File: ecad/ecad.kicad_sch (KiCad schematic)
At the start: 59 parts, among them J1 JTAG, J2 USB_C, SW1 Cherry MX, SW10 RotaryEncoder_Switch, SW11 RotaryEncoder_Switch, SW12 Cherry MX, SW13 Cherry MX, SW14 Cherry MX, SW15 RESET, SW2 Cherry MX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

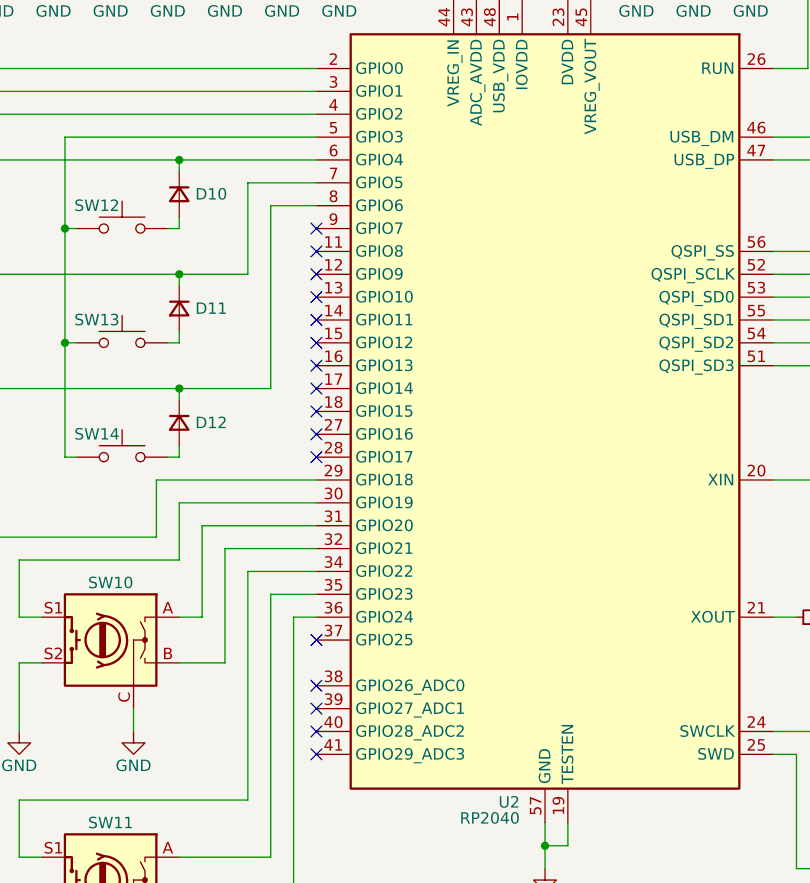
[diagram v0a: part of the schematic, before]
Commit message: feat(ecad): change pcb size to have constant margin
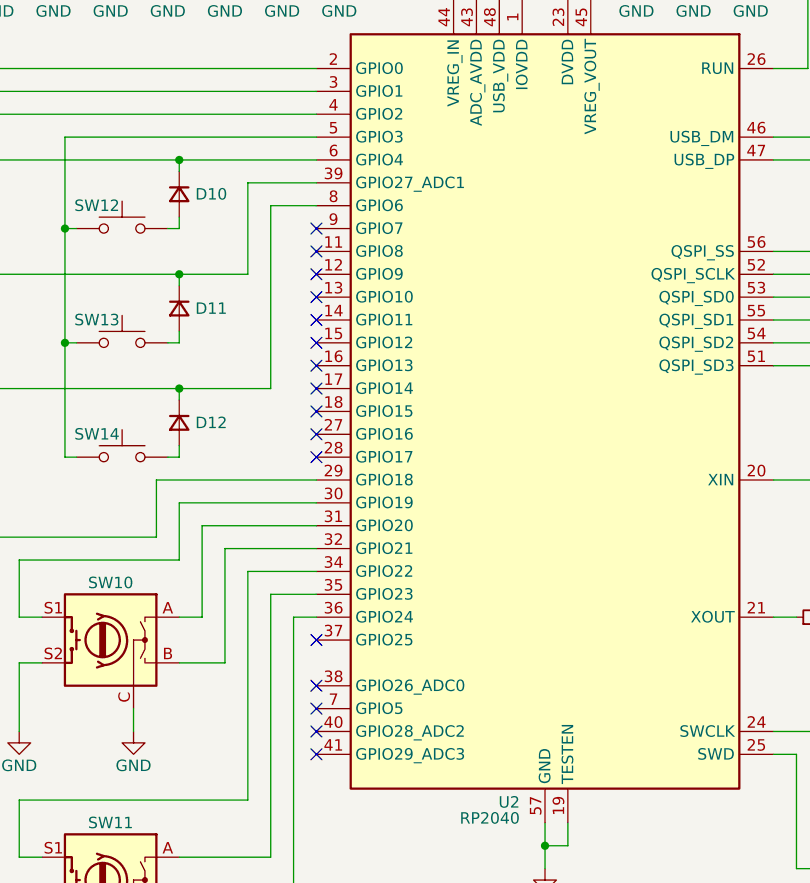
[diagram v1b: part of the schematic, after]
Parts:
- SW1, SW12, SW13, SW14, SW2, SW3, SW4, SW5, SW6, SW7, SW8, SW9: footprint PCM_Switch_Keyboard_Cherry_MX:SW_Cherry_MX_PCB_1.00u -> PCM_Switch_Keyboard_Hotswap_Kailh:SW_Hotswap_Kailh_Choc_V2
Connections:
- net at D11.1 (K), D2.1 (K), D5.1 (K)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: now also U2.39 (GPIO27_ADC1); no longer U2.7 (GPIO5)
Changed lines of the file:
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@@
 			)
 		)
-		(property "Footprint" "PCM_Switch_Keyboard_Cherry_MX:SW_Cherry_MX_PCB_1.00u"
+		(property "Footprint" "PCM_Switch_Keyboard_Hotswap_Kailh:SW_Hotswap_Kailh_Choc_V2"
 			(at 66.04 73.66 0)
 			(effects
@@
 			)
 		)
-		(property "Footprint" "PCM_Switch_Keyboard_Cherry_MX:SW_Cherry_MX_PCB_1.00u"
+		(property "Footprint" "PCM_Switch_Keyboard_Hotswap_Kailh:SW_Hotswap_Kailh_Choc_V2"
 			(at 66.04 60.96 0)
 			(effects
@@
 			)
 		)
-		(property "Footprint" "PCM_Switch_Keyboard_Cherry_MX:SW_Cherry_MX_PCB_1.00u"
+		(property "Footprint" "PCM_Switch_Keyboard_Hotswap_Kailh:SW_Hotswap_Kailh_Choc_V2"
 			(at 40.64 73.66 0)
 			(effects
@@
 			)
 		)
-		(property "Footprint" "PCM_Switch_Keyboard_Cherry_MX:SW_Cherry_MX_PCB_1.00u"
+		(property "Footprint" "PCM_Switch_Keyboard_Hotswap_Kailh:SW_Hotswap_Kailh_Choc_V2"
 			(at 91.44 86.36 0)
 			(effects
@@
 			)
 		)
-		(property "Footprint" "PCM_Switch_Keyboard_Cherry_MX:SW_Cherry_MX_PCB_1.00u"
+		(property "Footprint" "PCM_Switch_Keyboard_Hotswap_Kailh:SW_Hotswap_Kailh_Choc_V2"
 			(at 116.84 86.36 0)
 			(effects
@@
 			)
 		)
-		(property "Footprint" "PCM_Switch_Keyboard_Cherry_MX:SW_Cherry_MX_PCB_1.00u"
+		(property "Footprint" "PCM_Switch_Keyboard_Hotswap_Kailh:SW_Hotswap_Kailh_Choc_V2"
 			(at 116.84 60.96 0)
 			(effects
@@
 			)
 		)
-		(property "Footprint" "PCM_Switch_Keyboard_Cherry_MX:SW_Cherry_MX_PCB_1.00u"
+		(property "Footprint" "PCM_Switch_Keyboard_Hotswap_Kailh:SW_Hotswap_Kailh_Choc_V2"
 			(at 66.04 86.36 0)
 			(effects
@@
 			)
 		)
-		(property "Footprint" "PCM_Switch_Keyboard_Cherry_MX:SW_Cherry_MX_PCB_1.00u"
+		(property "Footprint" "PCM_Switch_Keyboard_Hotswap_Kailh:SW_Hotswap_Kailh_Choc_V2"
 			(at 116.84 73.66 0)
 			(effects
@@
 			)
 		)
-		(property "Footprint" "PCM_Switch_Keyboard_Cherry_MX:SW_Cherry_MX_PCB_1.00u"
+		(property "Footprint" "PCM_Switch_Keyboard_Hotswap_Kailh:SW_Hotswap_Kailh_Choc_V2"
 			(at 40.64 86.36 0)
 			(effects
@@
 			)
 		)
-		(property "Footprint" "PCM_Switch_Keyboard_Cherry_MX:SW_Cherry_MX_PCB_1.00u"
+		(property "Footprint" "PCM_Switch_Keyboard_Hotswap_Kailh:SW_Hotswap_Kailh_Choc_V2"
 			(at 91.44 60.96 0)
 			(effects
@@
 			)
 		)
-		(property "Footprint" "PCM_Switch_Keyboard_Cherry_MX:SW_Cherry_MX_PCB_1.00u"
+		(property "Footprint" "PCM_Switch_Keyboard_Hotswap_Kailh:SW_Hotswap_Kailh_Choc_V2"
 			(at 40.64 60.96 0)
 			(effects
@@
 			)
 		)
-		(property "Footprint" "PCM_Switch_Keyboard_Cherry_MX:SW_Cherry_MX_PCB_1.00u"
+		(property "Footprint" "PCM_Switch_Keyboard_Hotswap_Kailh:SW_Hotswap_Kailh_Choc_V2"
 			(at 91.44 73.66 0)
 			(effects

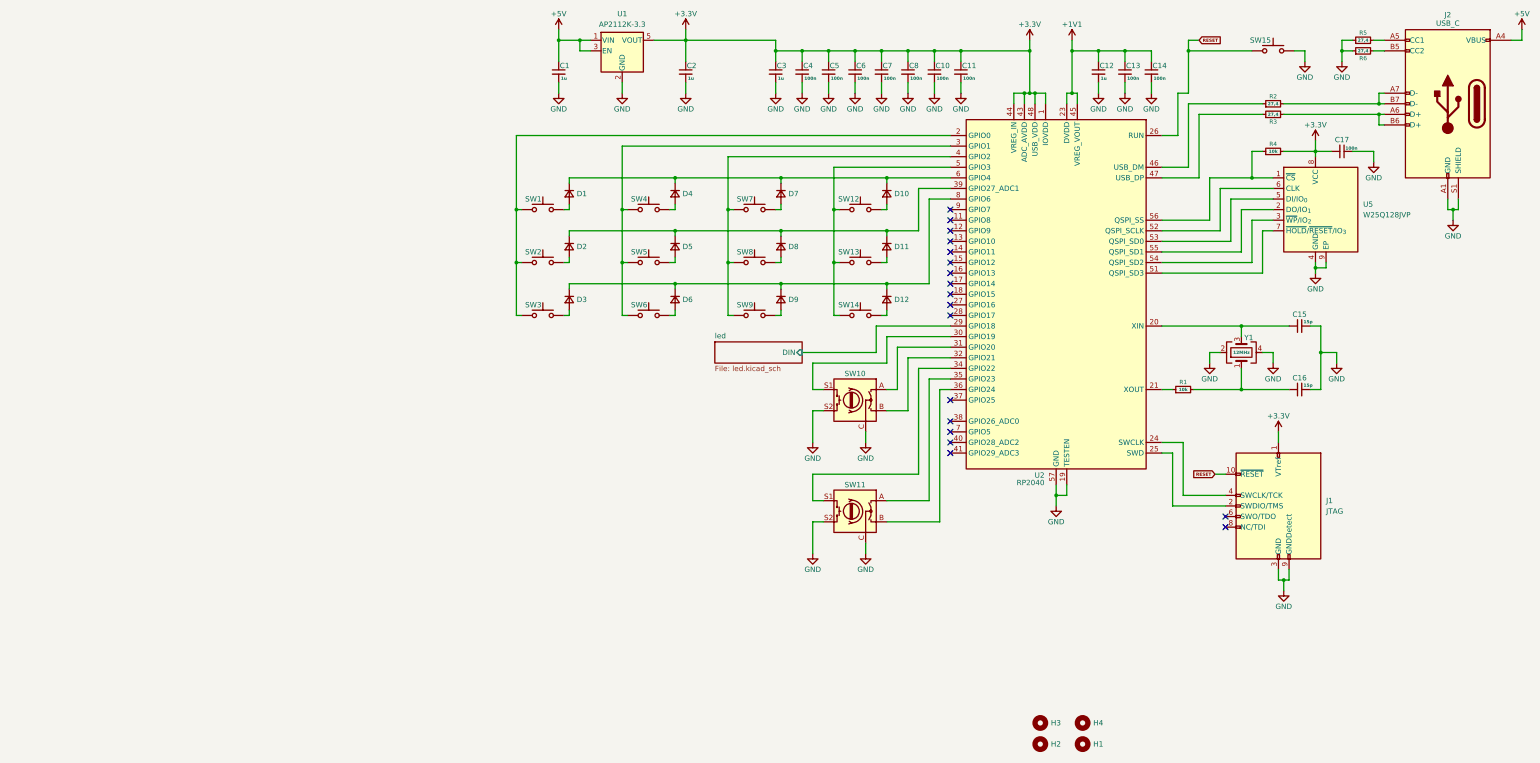
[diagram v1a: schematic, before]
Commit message: fix(ecad): change pcb format
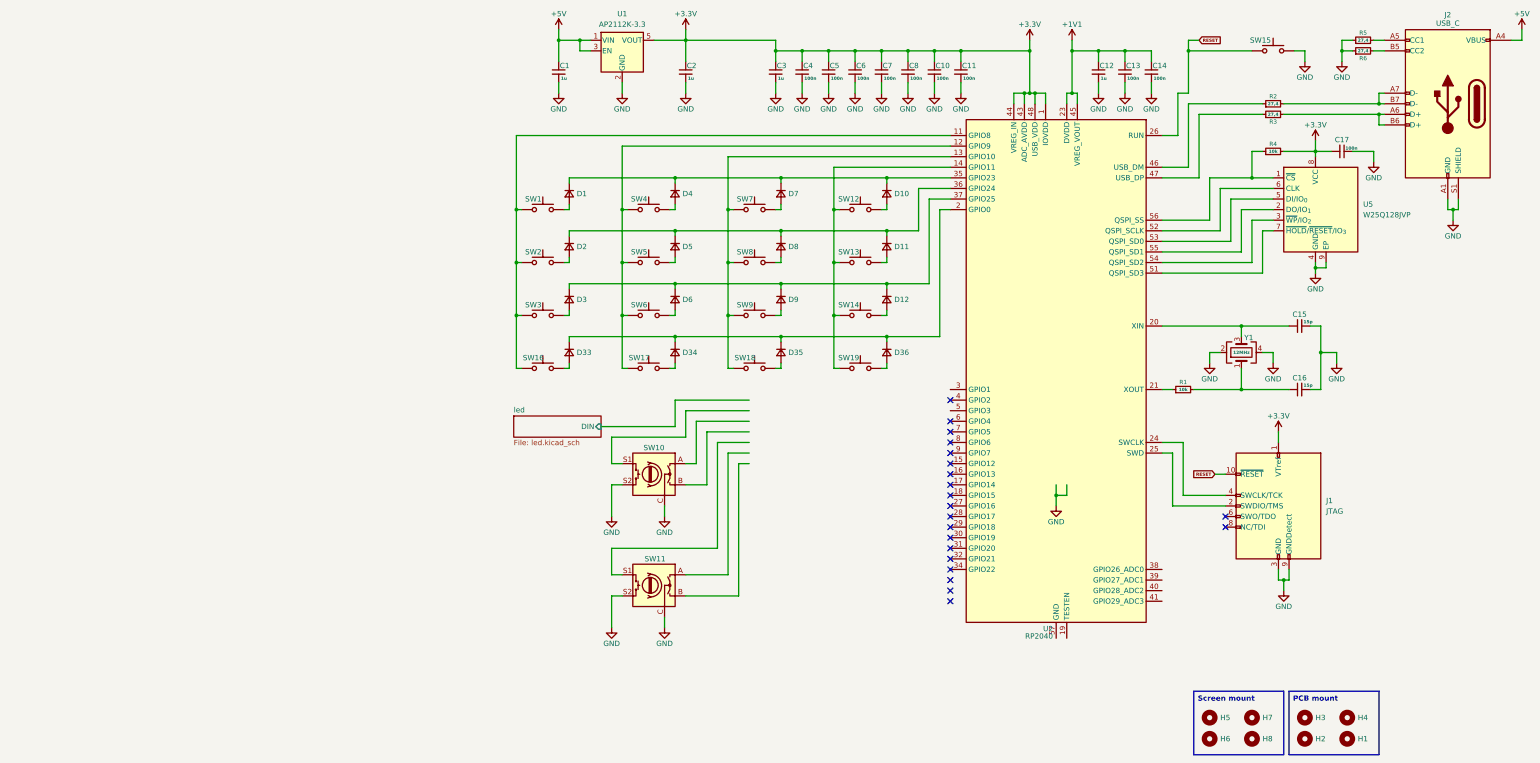
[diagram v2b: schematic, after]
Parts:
- added D33, D34, D35, D36: D_Small, Diode_SMD:D_0402_1005Metric, symbol Device:D_Small
- added H5, H6, H7, H8: MountingHole, MountingHole:MountingHole_2.2mm_M2_DIN965_Pad, symbol Mechanical:MountingHole
- added SW16, SW17, SW18, SW19: Kailh choc v2, PCM_Switch_Keyboard_Hotswap_Kailh:SW_Hotswap_Kailh_Choc_V2, symbol Switch:SW_Push
- H1, H2, H3, H4: footprint MountingHole:MountingHole_2.2mm_M2_DIN965_Pad -> MountingHole:MountingHole_2.2mm_M2_DIN965
- SW1, SW12, SW13, SW14, SW2, SW3, SW4, SW5, SW6, SW7, SW8, SW9: value Cherry MX -> Kailh choc v2
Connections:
- net GND: no longer U2.19 (TESTEN), U2.57 (GND)
- net led/DIN: no longer U2.29 (GPIO18)
- net at SW4.1, SW5.1, SW6.1: now also U2.12 (GPIO9), SW17.1; no longer U2.3 (GPIO1)
- net at D12.1 (K), D3.1 (K), D6.1 (K)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: now also U2.37 (GPIO25); no longer U2.8 (GPIO6)
- net at D11.1 (K), D2.1 (K), D5.1 (K)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: now also U2.36 (GPIO24); no longer U2.39 (GPIO27_ADC1)
- net at SW1.1, SW2.1, SW3.1: now also U2.11 (GPIO8), SW16.1; no longer U2.2 (GPIO0)
- net at SW7.1, SW8.1, SW9.1: now also U2.13 (GPIO10), SW18.1; no longer U2.4 (GPIO2)
- net at D1.1 (K), D10.1 (K), D4.1 (K)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: now also U2.35 (GPIO23); no longer U2.6 (GPIO4)
- net at SW12.1, SW13.1, SW14.1: now also U2.14 (GPIO11), SW19.1; no longer U2.5 (GPIO3)
- net at U2.30 (GPIO19): no longer SW10.S1
- net at U2.31 (GPIO20): no longer SW10.A
- net at U2.32 (GPIO21): no longer SW10.B
- net at U2.34 (GPIO22): no longer SW11.S1
- net at SW11.A: no longer U2.35 (GPIO23)
- net at SW11.B: no longer U2.36 (GPIO24)
- new net: D33.1 (K), D34.1 (K), D35.1 (K), D36.1 (K), U2.2 (GPIO0)
- new net: D35.2 (A), SW18.2
- new net: D33.2 (A), SW16.2
- new net: D34.2 (A), SW17.2
- new net: D36.2 (A), SW19.2
- no-connect marks 18 -> 21
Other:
- moved on the sheet: H1, H2, H4, SW10, SW11, U2

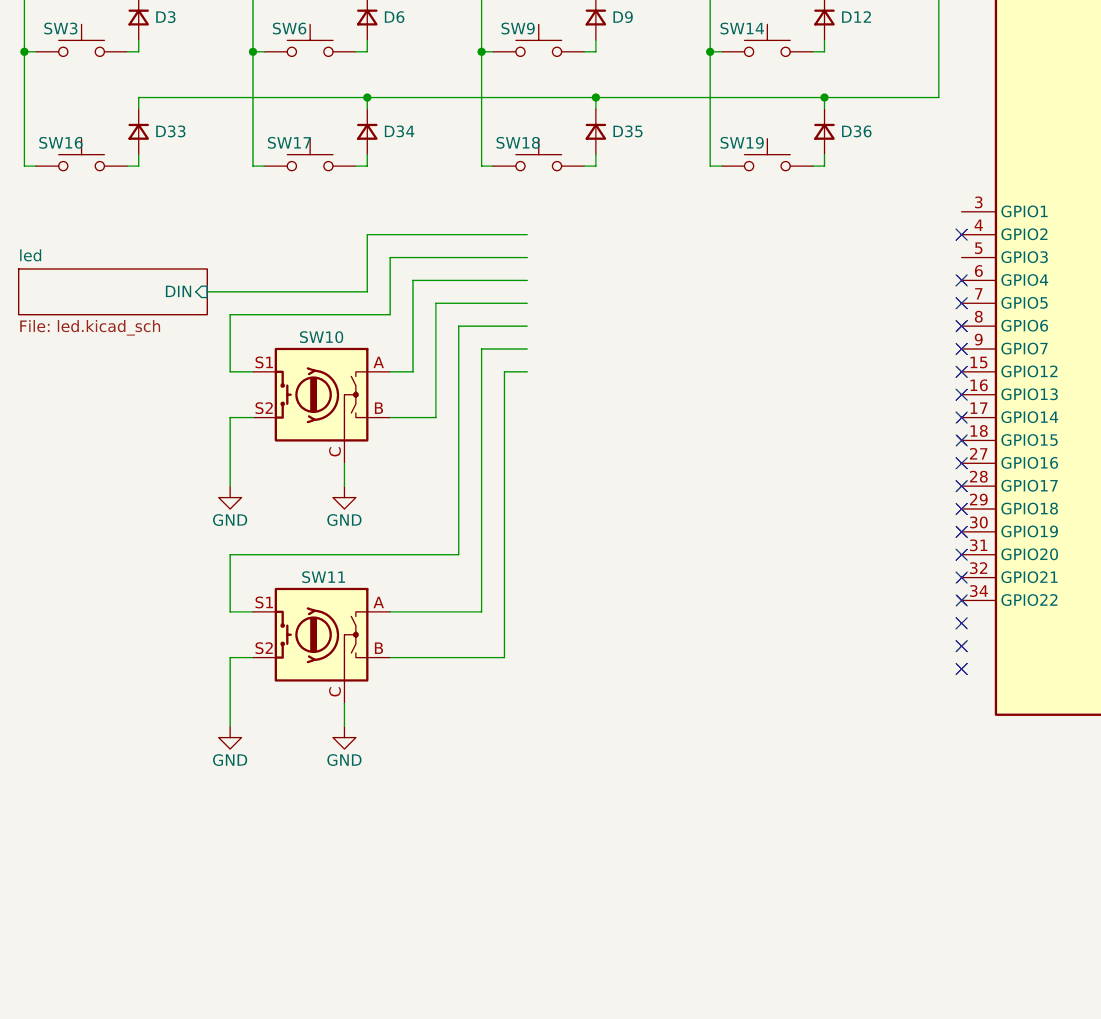
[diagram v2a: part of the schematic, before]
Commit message: fix(ecad): replace components to fit new format
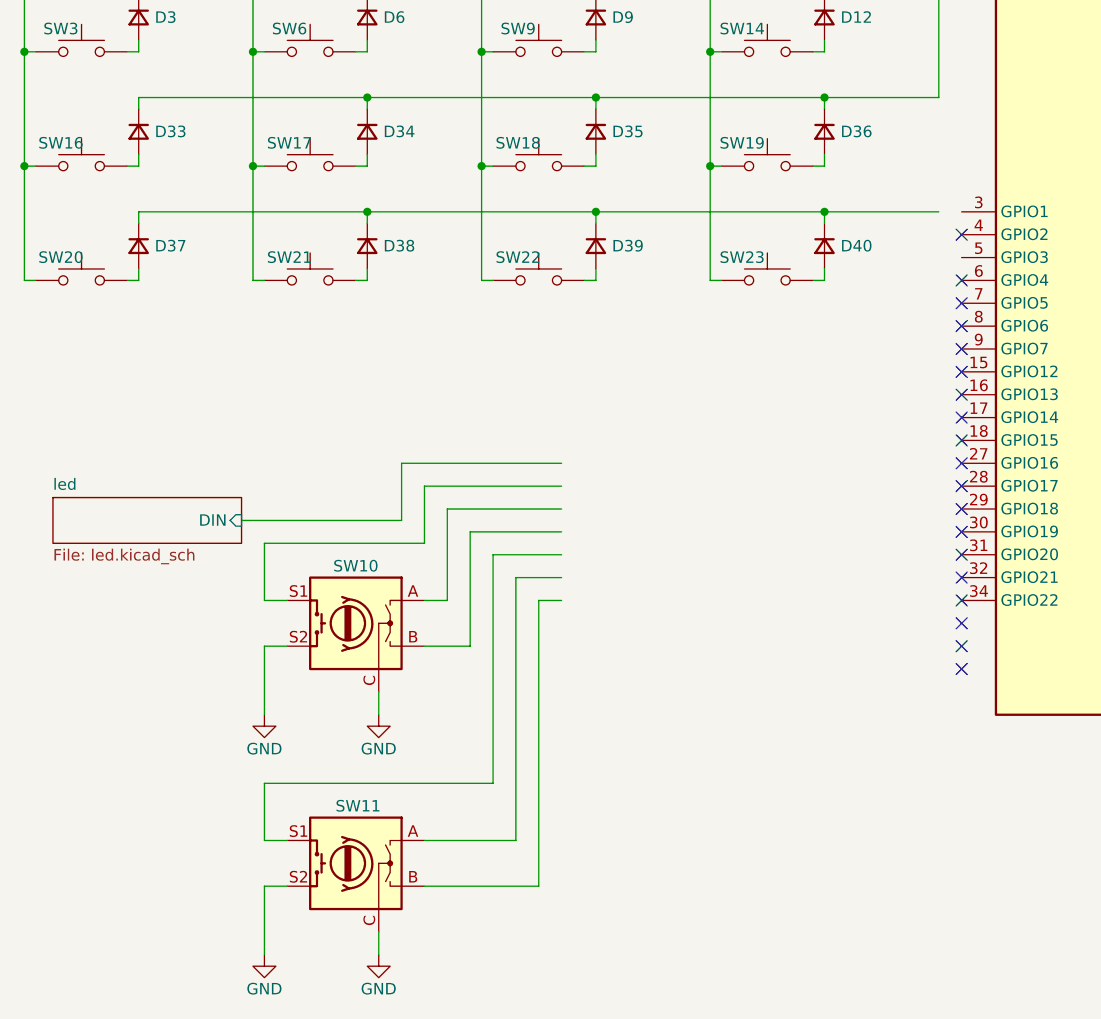
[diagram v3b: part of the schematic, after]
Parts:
- added D37, D38, D39, D40: D_Small, Diode_SMD:D_0402_1005Metric, symbol Device:D_Small
- added SW20, SW21, SW22, SW23: Kailh choc v2, PCM_Switch_Keyboard_Hotswap_Kailh:SW_Hotswap_Kailh_Choc_V2, symbol Switch:SW_Push
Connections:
- net at SW18.1, SW7.1, SW8.1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: now also SW22.1
- net at SW17.1, SW4.1, SW5.1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: now also SW21.1
- net at SW1.1, SW16.1, SW2.1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: now also SW20.1
- net at SW12.1, SW13.1, SW14.1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: now also SW23.1
- new net: D38.2 (A), SW21.2
- new net: D37.1 (K), D38.1 (K), D39.1 (K), D40.1 (K)
- new net: D40.2 (A), SW23.2
- new net: D39.2 (A), SW22.2
- new net: D37.2 (A), SW20.2
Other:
- moved on the sheet: SW10, SW11
